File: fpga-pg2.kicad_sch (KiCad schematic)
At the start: 1 part, among them U6 XC7A15T-CSG325

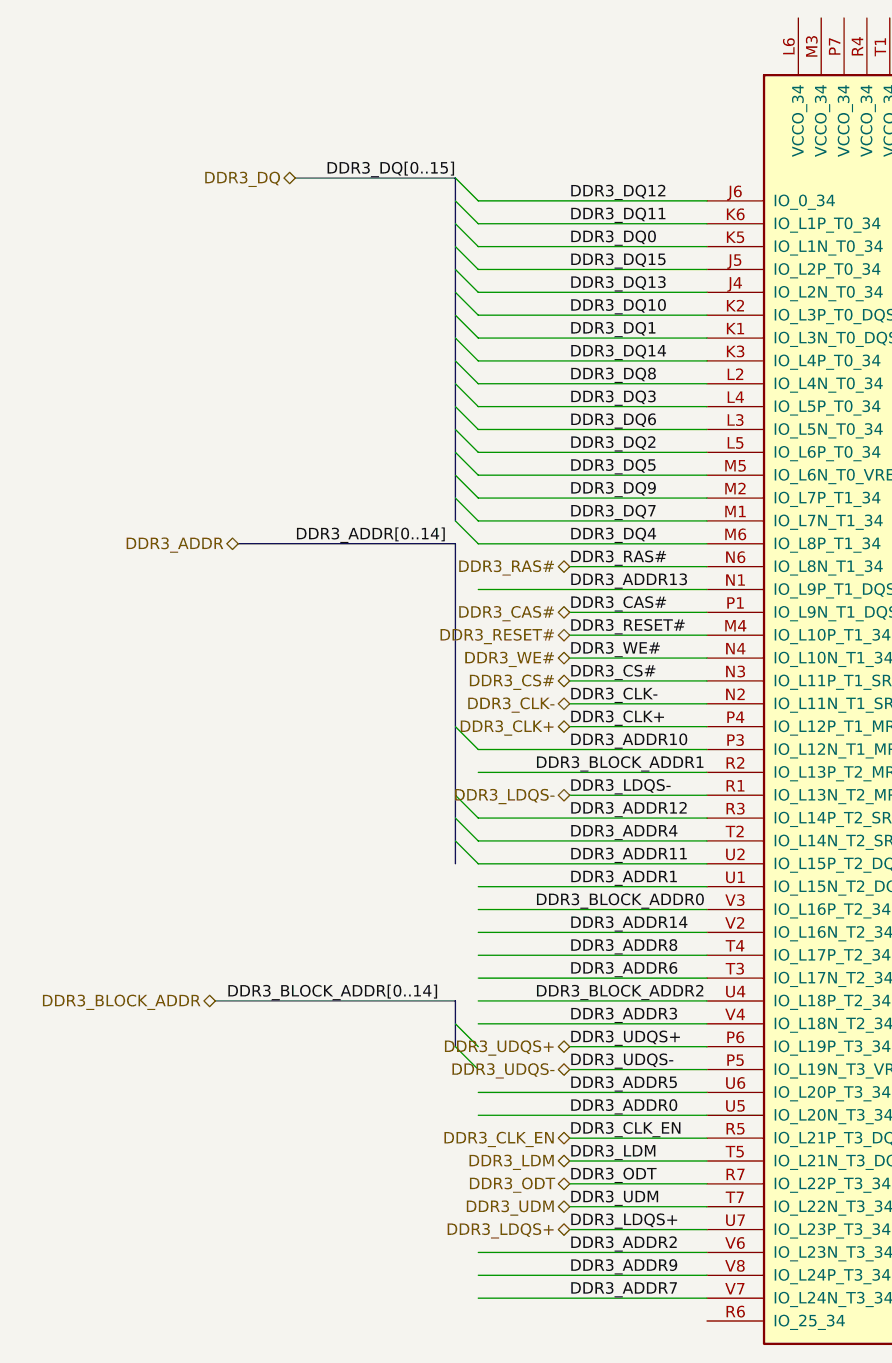
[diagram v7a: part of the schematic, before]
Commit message: changed ddr3 pinning according to hard-ip in vivado
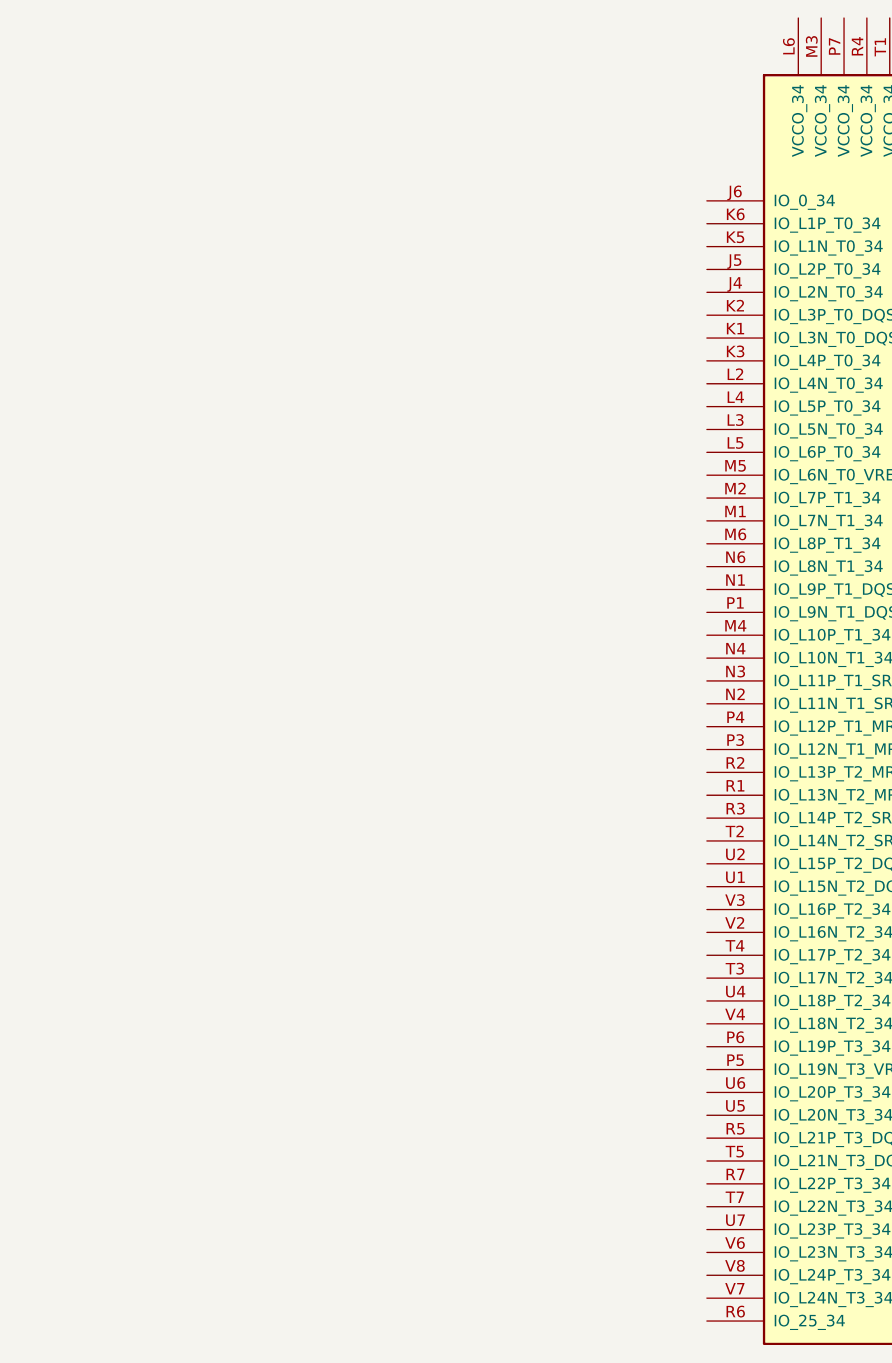
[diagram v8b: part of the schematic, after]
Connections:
- net DDR3_ADDR0: no longer names the net of U6.U5 (IO_L20N_T3_34)
- net DDR3_ADDR1: no longer names the net of U6.U1 (IO_L15N_T2_DQS_34)
- net DDR3_ADDR10: no longer names the net of U6.P3 (IO_L12N_T1_MRCC_34)
- net DDR3_ADDR11: no longer names the net of U6.U2 (IO_L15P_T2_DQS_34)
- net DDR3_ADDR12: no longer names the net of U6.R3 (IO_L14P_T2_SRCC_34)
- net DDR3_ADDR13: no longer names the net of U6.N1 (IO_L9P_T1_DQS_34)
- net DDR3_ADDR14: no longer names the net of U6.V2 (IO_L16N_T2_34)
- net DDR3_ADDR2: no longer names the net of U6.V6 (IO_L23N_T3_34)
- net DDR3_ADDR3: no longer names the net of U6.V4 (IO_L18N_T2_34)
- net DDR3_ADDR4: no longer names the net of U6.T2 (IO_L14N_T2_SRCC_34)
- net DDR3_ADDR5: no longer names the net of U6.U6 (IO_L20P_T3_34)
- net DDR3_ADDR6: no longer names the net of U6.T3 (IO_L17N_T2_34)
- net DDR3_ADDR7: no longer names the net of U6.V7 (IO_L24N_T3_34)
- net DDR3_ADDR8: no longer names the net of U6.T4 (IO_L17P_T2_34)
- net DDR3_ADDR9: no longer names the net of U6.V8 (IO_L24P_T3_34)
- net DDR3_BLOCK_ADDR0: no longer names the net of U6.V3 (IO_L16P_T2_34)
- net DDR3_BLOCK_ADDR1: no longer names the net of U6.R2 (IO_L13P_T2_MRCC_34)
- net DDR3_BLOCK_ADDR2: no longer names the net of U6.U4 (IO_L18P_T2_34)
- net DDR3_CAS#: no longer names the net of U6.P1 (IO_L9N_T1_DQS_34)
- net DDR3_CLK+: no longer names the net of U6.P4 (IO_L12P_T1_MRCC_34)
- net DDR3_CLK-: no longer names the net of U6.N2 (IO_L11N_T1_SRCC_34)
- net DDR3_CLK_EN: no longer names the net of U6.R5 (IO_L21P_T3_DQS_34)
- net DDR3_CS#: no longer names the net of U6.N3 (IO_L11P_T1_SRCC_34)
- net DDR3_DQ0: no longer names the net of U6.K5 (IO_L1N_T0_34)
- net DDR3_DQ1: no longer names the net of U6.K1 (IO_L3N_T0_DQS_34)
- net DDR3_DQ10: no longer names the net of U6.K2 (IO_L3P_T0_DQS_34)
- net DDR3_DQ11: no longer names the net of U6.K6 (IO_L1P_T0_34)
- net DDR3_DQ12: no longer names the net of U6.J6 (IO_0_34)
- net DDR3_DQ13: no longer names the net of U6.J4 (IO_L2N_T0_34)
- net DDR3_DQ14: no longer names the net of U6.K3 (IO_L4P_T0_34)
- net DDR3_DQ15: no longer names the net of U6.J5 (IO_L2P_T0_34)
- net DDR3_DQ2: no longer names the net of U6.L5 (IO_L6P_T0_34)
- net DDR3_DQ3: no longer names the net of U6.L4 (IO_L5P_T0_34)
- net DDR3_DQ4: no longer names the net of U6.M6 (IO_L8P_T1_34)
- net DDR3_DQ5: no longer names the net of U6.M5 (IO_L6N_T0_VREF_34)
- net DDR3_DQ6: no longer names the net of U6.L3 (IO_L5N_T0_34)
- net DDR3_DQ7: no longer names the net of U6.M1 (IO_L7N_T1_34)
- net DDR3_DQ8: no longer names the net of U6.L2 (IO_L4N_T0_34)
- net DDR3_DQ9: no longer names the net of U6.M2 (IO_L7P_T1_34)
- net DDR3_LDM: no longer names the net of U6.T5 (IO_L21N_T3_DQS_34)
- net DDR3_LDQS+: no longer names the net of U6.U7 (IO_L23P_T3_34)
- net DDR3_LDQS-: no longer names the net of U6.R1 (IO_L13N_T2_MRCC_34)
- net DDR3_ODT: no longer names the net of U6.R7 (IO_L22P_T3_34)
- net DDR3_RAS#: no longer names the net of U6.N6 (IO_L8N_T1_34)
- net DDR3_RESET#: no longer names the net of U6.M4 (IO_L10P_T1_34)
- net DDR3_UDM: no longer names the net of U6.T7 (IO_L22N_T3_34)
- net DDR3_UDQS+: no longer names the net of U6.P6 (IO_L19P_T3_34)
- net DDR3_UDQS-: no longer names the net of U6.P5 (IO_L19N_T3_VREF_34)
- net DDR3_WE#: no longer names the net of U6.N4 (IO_L10N_T1_34)
